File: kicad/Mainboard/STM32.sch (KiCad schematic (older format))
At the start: 30 parts, among them J1 TP1, J11 VIB2, J2 TP2, J3 USB_OTG, J4 SWD, J9 VIB1, Q1 BSS138, Q6 BSS138, U1 STM32F777VIT, U2 USBLC6-2SC6

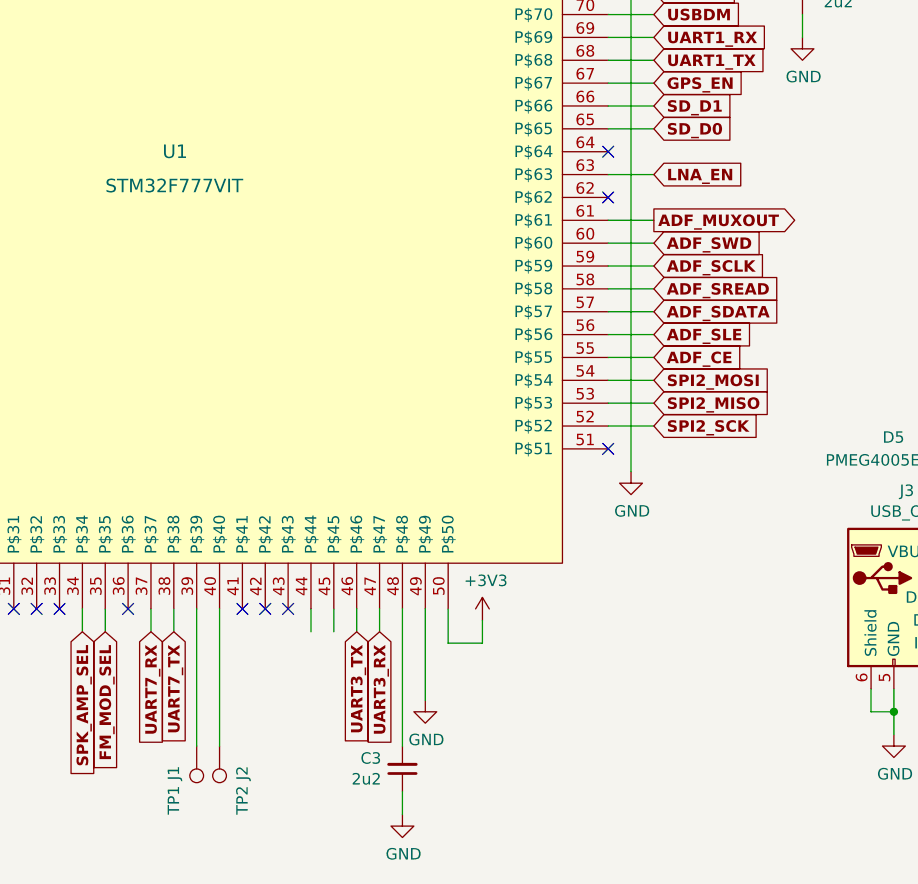
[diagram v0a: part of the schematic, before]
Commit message: Added some vias and forgotten power supply lines & plotted pdf schematic
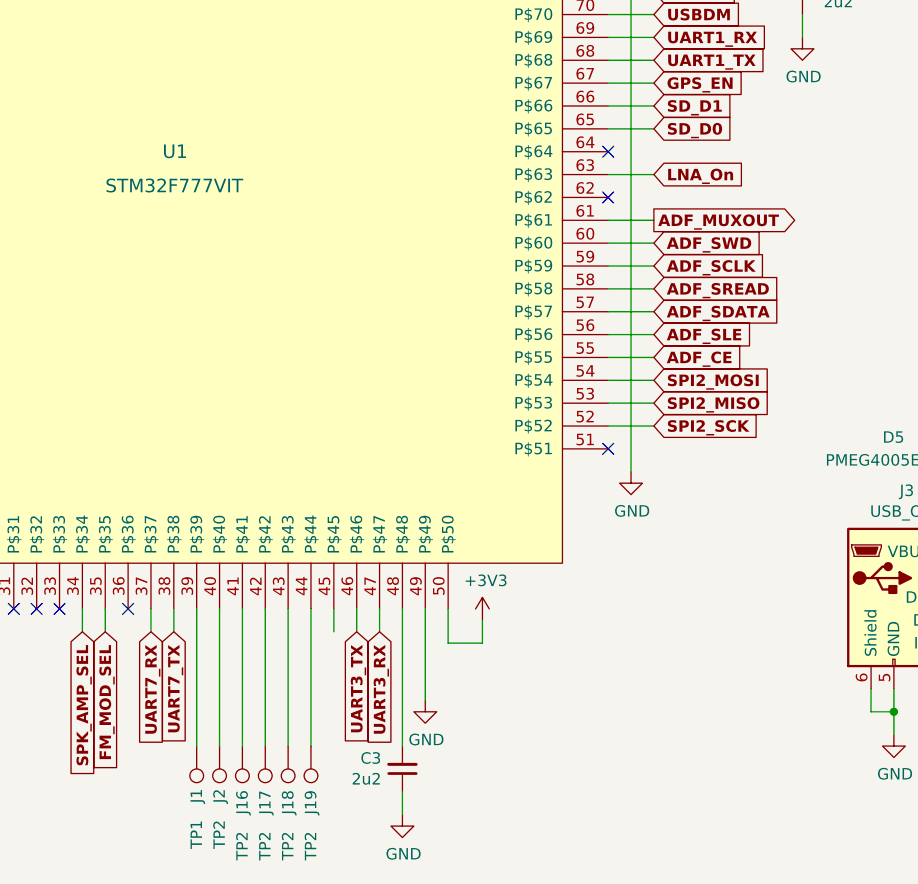
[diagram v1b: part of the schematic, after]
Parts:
- added J16, J17, J18, J19: TP2, TestPoint:TestPoint_Pad_D1.0mm, symbol Mainboard-rescue:TEST_1P-conn
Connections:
- net at U1.41 (P$41): now also J16.1
- net at U1.42 (P$42): now also J17.1
- net at U1.43 (P$43): now also J18.1
- net at U1.44 (P$44): now also J19.1
- net LNA_EN renamed LNA_On
- no-connect marks 28 -> 25
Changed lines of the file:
@@
 EESchema Schematic File Version 4
-LIBS:Mainboard-cache
 EELAYER 30 0
 EELAYER END
@@
 U 1 1 5DE542F9
 P 5100 5950
-F 0 "J1" V 5200 6100 50  0000 R CNN
-F 1 "TP1" V 5200 6250 50  0000 R CNN
+F 0 "J1" V 5100 6200 50  0000 R CNN
+F 1 "TP1" V 5100 6400 50  0000 R CNN
 F 2 "TestPoint:TestPoint_Pad_D1.0mm" H 5300 5950 50  0001 C CNN
 F 3 "" H 5300 5950 50  0001 C CNN
@@
 U 1 1 5DE55232
 P 5200 5950
-F 0 "J2" V 5300 6100 50  0000 R CNN
-F 1 "TP2" V 5300 6250 50  0000 R CNN
+F 0 "J2" V 5200 6200 50  0000 R CNN
+F 1 "TP2" V 5200 6400 50  0000 R CNN
 F 2 "TestPoint:TestPoint_Pad_D1.0mm" H 5400 5950 50  0001 C CNN
 F 3 "" H 5400 5950 50  0001 C CNN
@@
 NoConn ~ 4500 5350
 NoConn ~ 4800 5350
-NoConn ~ 5300 5350
-NoConn ~ 5400 5350
-NoConn ~ 5500 5350
 Wire Wire Line
 	6900 2350 7000 2350
@@
 Wire Wire Line
 	5200 5350 5200 5950
-Wire Wire Line
-	5600 5450 5600 5350
 Text GLabel 4300 1450 1    50   Input ~ 10
 WIFI_RST
@@
 	8500 1300 8600 1300
 Text GLabel 7100 3450 2    50   Input ~ 10
-LNA_EN
+LNA_On
 Wire Wire Line
 	7100 3450 6900 3450
 Wire Wire Line
 	6900 3650 7100 3650
+$Comp
+L Mainboard-rescue:TEST_1P-conn J16
+U 1 1 5EDA6785
+P 5300 5950
+F 0 "J16" V 5300 6250 50  0000 R CNN
+F 1 "TP2" V 5300 6450 50  0000 R CNN
+F 2 "TestPoint:TestPoint_Pad_D1.0mm" H 5500 5950 50  0001 C CNN
+F 3 "" H 5500 5950 50  0001 C CNN
+	1    5300 5950
+	1    0    0    1
+$EndComp
+$Comp
+L Mainboard-rescue:TEST_1P-conn J17
+U 1 1 5EDA8668
+P 5400 5950
+F 0 "J17" V 5400 6250 50  0000 R CNN
+F 1 "TP2" V 5400 6450 50  0000 R CNN
+F 2 "TestPoint:TestPoint_Pad_D1.0mm" H 5600 5950 50  0001 C CNN
+F 3 "" H 5600 5950 50  0001 C CNN
+	1    5400 5950
+	1    0    0    1
+$EndComp
+$Comp
+L Mainboard-rescue:TEST_1P-conn J18
+U 1 1 5EDA889B
+P 5500 5950
+F 0 "J18" V 5500 6250 50  0000 R CNN
+F 1 "TP2" V 5500 6450 50  0000 R CNN
+F 2 "TestPoint:TestPoint_Pad_D1.0mm" H 5700 5950 50  0001 C CNN
+F 3 "" H 5700 5950 50  0001 C CNN
+	1    5500 5950
+	1    0    0    1
+$EndComp
+$Comp
+L Mainboard-rescue:TEST_1P-conn J19
+U 1 1 5EDA8A58
+P 5600 5950
+F 0 "J19" V 5600 6250 50  0000 R CNN
+F 1 "TP2" V 5600 6450 50  0000 R CNN
+F 2 "TestPoint:TestPoint_Pad_D1.0mm" H 5800 5950 50  0001 C CNN
+F 3 "" H 5800 5950 50  0001 C CNN
+	1    5600 5950
+	1    0    0    1
+$EndComp
+Wire Wire Line
+	5300 5350 5300 5950
+Wire Wire Line
+	5400 5950 5400 5350
+Wire Wire Line
+	5500 5350 5500 5950
+Wire Wire Line
+	5600 5350 5600 5950
 $EndSCHEMATC

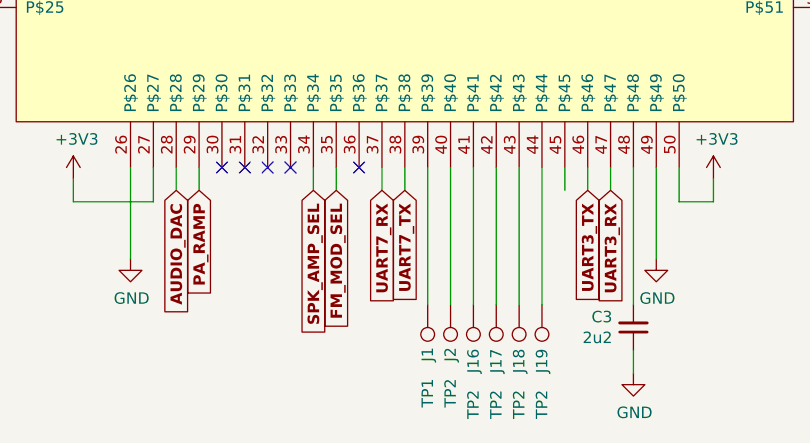
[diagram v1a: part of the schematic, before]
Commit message: added 9 TestPoints called N1 ... to N9, which allow to debug STM32, and experiment with more peripherals in the future. Plotted PDF schematic
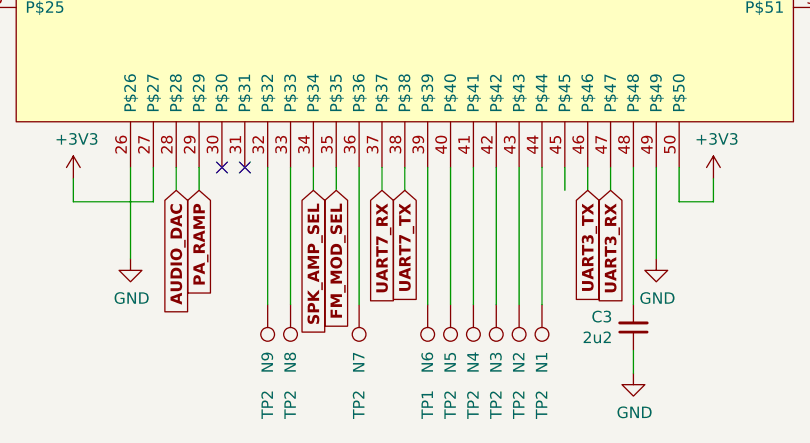
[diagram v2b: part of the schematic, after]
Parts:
- added N7, N8, N9: TP2, TestPoint:TestPoint_Pad_D1.0mm, symbol Mainboard-rescue:TEST_1P-conn
- renumbered J19 to N1, J18 to N2, J17 to N3, J16 to N4, J2 to N5, J1 to N6
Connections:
- net at U1.32 (P$32): now also N9.1
- net at U1.33 (P$33): now also N8.1
- net at U1.36 (P$36): now also N7.1
- no-connect marks 25 -> 22
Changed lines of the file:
@@
 	5900 5350 5900 5450
 $Comp
-L Mainboard-rescue:TEST_1P-conn J1
+L Mainboard-rescue:TEST_1P-conn N6
 U 1 1 5DE542F9
 P 5100 5950
-F 0 "J1" V 5100 6200 50  0000 R CNN
-F 1 "TP1" V 5100 6400 50  0000 R CNN
+F 0 "N6" V 5100 6250 50  0000 R CNN
+F 1 "TP1" V 5100 6450 50  0000 R CNN
 F 2 "TestPoint:TestPoint_Pad_D1.0mm" H 5300 5950 50  0001 C CNN
 F 3 "" H 5300 5950 50  0001 C CNN
@@
 $EndComp
 $Comp
-L Mainboard-rescue:TEST_1P-conn J2
+L Mainboard-rescue:TEST_1P-conn N5
 U 1 1 5DE55232
 P 5200 5950
-F 0 "J2" V 5200 6200 50  0000 R CNN
-F 1 "TP2" V 5200 6400 50  0000 R CNN
+F 0 "N5" V 5200 6250 50  0000 R CNN
+F 1 "TP2" V 5200 6450 50  0000 R CNN
 F 2 "TestPoint:TestPoint_Pad_D1.0mm" H 5400 5950 50  0001 C CNN
 F 3 "" H 5400 5950 50  0001 C CNN
@@
 Wire Wire Line
 	3800 5350 3800 5750
-NoConn ~ 4500 5350
-NoConn ~ 4800 5350
 Wire Wire Line
 	6900 2350 7000 2350
@@
 NoConn ~ 4200 5350
 NoConn ~ 4300 5350
-NoConn ~ 4400 5350
 Wire Wire Line
 	4800 1450 4800 1550
@@
 	6900 3650 7100 3650
 $Comp
-L Mainboard-rescue:TEST_1P-conn J16
+L Mainboard-rescue:TEST_1P-conn N4
 U 1 1 5EDA6785
 P 5300 5950
-F 0 "J16" V 5300 6250 50  0000 R CNN
+F 0 "N4" V 5300 6250 50  0000 R CNN
 F 1 "TP2" V 5300 6450 50  0000 R CNN
 F 2 "TestPoint:TestPoint_Pad_D1.0mm" H 5500 5950 50  0001 C CNN
@@
 $EndComp
 $Comp
-L Mainboard-rescue:TEST_1P-conn J17
+L Mainboard-rescue:TEST_1P-conn N3
 U 1 1 5EDA8668
 P 5400 5950
-F 0 "J17" V 5400 6250 50  0000 R CNN
+F 0 "N3" V 5400 6250 50  0000 R CNN
 F 1 "TP2" V 5400 6450 50  0000 R CNN
 F 2 "TestPoint:TestPoint_Pad_D1.0mm" H 5600 5950 50  0001 C CNN
@@
 $EndComp
 $Comp
-L Mainboard-rescue:TEST_1P-conn J18
+L Mainboard-rescue:TEST_1P-conn N2
 U 1 1 5EDA889B
 P 5500 5950
-F 0 "J18" V 5500 6250 50  0000 R CNN
+F 0 "N2" V 5500 6250 50  0000 R CNN
 F 1 "TP2" V 5500 6450 50  0000 R CNN
 F 2 "TestPoint:TestPoint_Pad_D1.0mm" H 5700 5950 50  0001 C CNN
@@
 $EndComp
 $Comp
-L Mainboard-rescue:TEST_1P-conn J19
+L Mainboard-rescue:TEST_1P-conn N1
 U 1 1 5EDA8A58
 P 5600 5950
-F 0 "J19" V 5600 6250 50  0000 R CNN
+F 0 "N1" V 5600 6250 50  0000 R CNN
 F 1 "TP2" V 5600 6450 50  0000 R CNN
 F 2 "TestPoint:TestPoint_Pad_D1.0mm" H 5800 5950 50  0001 C CNN
@@
 Wire Wire Line
 	5600 5350 5600 5950
+$Comp
+L Mainboard-rescue:TEST_1P-conn N7
+U 1 1 5EE3107D
+P 4800 5950
+F 0 "N7" V 4800 6250 50  0000 R CNN
+F 1 "TP2" V 4800 6450 50  0000 R CNN
+F 2 "TestPoint:TestPoint_Pad_D1.0mm" H 5000 5950 50  0001 C CNN
+F 3 "" H 5000 5950 50  0001 C CNN
+	1    4800 5950
+	1    0    0    1
+$EndComp
+$Comp
+L Mainboard-rescue:TEST_1P-conn N8
+U 1 1 5EE31358
+P 4500 5950
+F 0 "N8" V 4500 6250 50  0000 R CNN
+F 1 "TP2" V 4500 6450 50  0000 R CNN
+F 2 "TestPoint:TestPoint_Pad_D1.0mm" H 4700 5950 50  0001 C CNN
+F 3 "" H 4700 5950 50  0001 C CNN
+	1    4500 5950
+	1    0    0    1
+$EndComp
+$Comp
+L Mainboard-rescue:TEST_1P-conn N9
+U 1 1 5EE317B2
+P 4400 5950
+F 0 "N9" V 4400 6250 50  0000 R CNN
+F 1 "TP2" V 4400 6450 50  0000 R CNN
+F 2 "TestPoint:TestPoint_Pad_D1.0mm" H 4600 5950 50  0001 C CNN
+F 3 "" H 4600 5950 50  0001 C CNN
+	1    4400 5950
+	1    0    0    1
+$EndComp
+Wire Wire Line
+	4800 5350 4800 5950
+Wire Wire Line
+	4500 5350 4500 5950
+Wire Wire Line
+	4400 5350 4400 5950
 $EndSCHEMATC

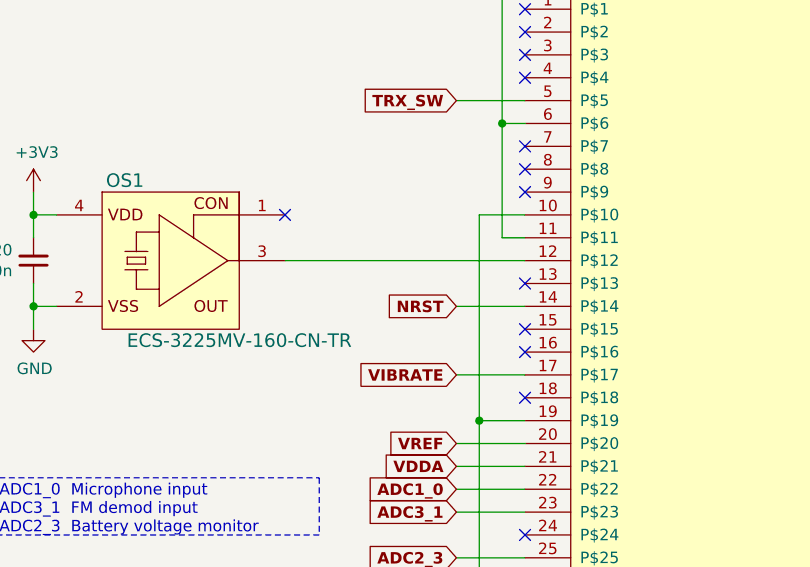
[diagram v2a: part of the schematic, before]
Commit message: added jumpers on GPIO0 and GPIO2 for ESP8266 module; described pin headers on PCB; connected pin 16 of STM32 to Power Down pin in OS1; plotted schematic in PDF
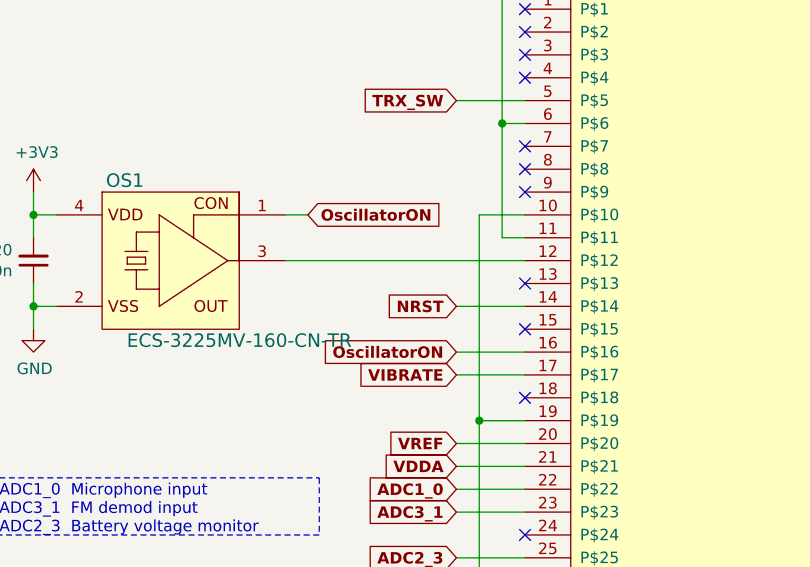
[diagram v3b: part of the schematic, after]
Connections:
- net OscillatorON: now reaches OS1.1 (CON)
- net OscillatorON: now also U1.16 (P$16)
- no-connect marks 22 -> 20
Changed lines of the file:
@@
 	1    0    0    -1
 $EndComp
-NoConn ~ 2050 3150
 $Comp
 L TR-9:STM32F777VIT U1
@@
 NoConn ~ 3100 3450
 NoConn ~ 3100 3650
-NoConn ~ 3100 3750
 NoConn ~ 3100 3950
 NoConn ~ 3100 4550
@@
 Wire Wire Line
 	4400 5350 4400 5950
+Text GLabel 2800 3750 0    50   Input ~ 10
+OscillatorON
+Wire Wire Line
+	3100 3750 2800 3750
+Text GLabel 2150 3150 2    50   Input ~ 10
+OscillatorON
+Wire Wire Line
+	2150 3150 2050 3150
 $EndSCHEMATC

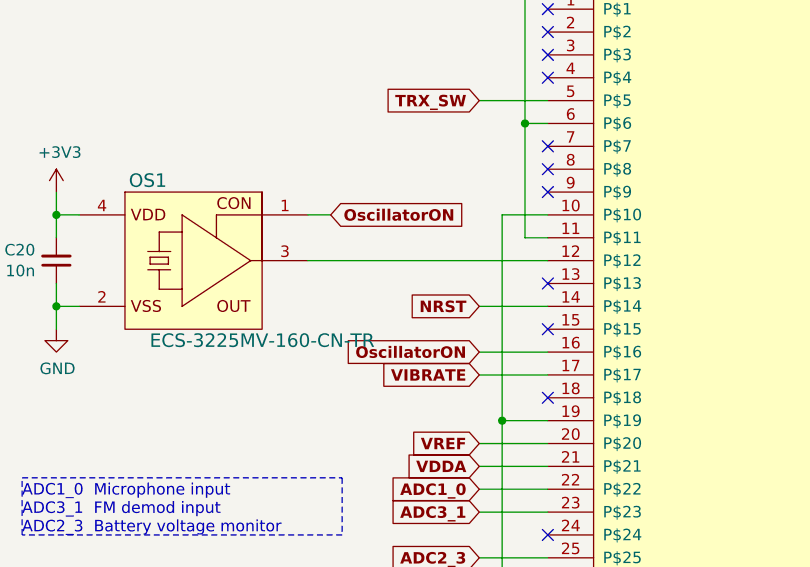
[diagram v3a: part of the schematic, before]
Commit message: changed OscillatorON to XO_EN -> added "SN:" title on PCB -> plotted new PDF
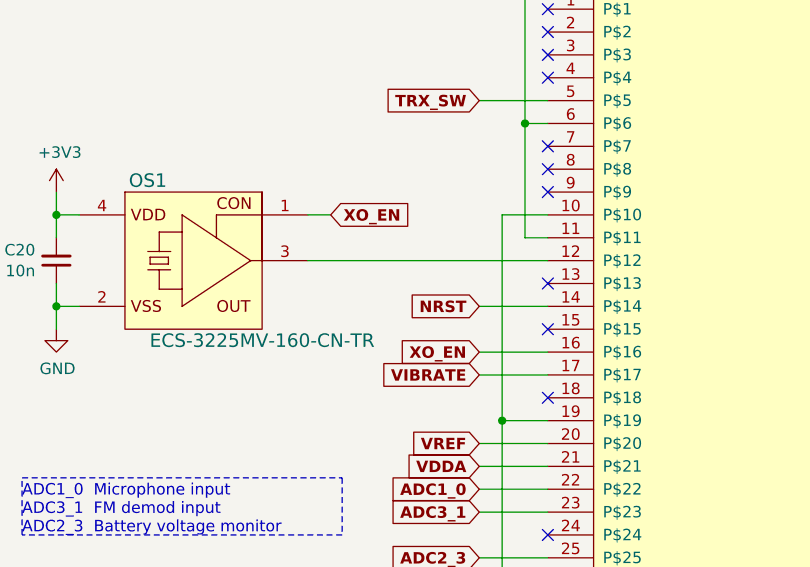
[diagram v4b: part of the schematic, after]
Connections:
- net OscillatorON renamed XO_EN
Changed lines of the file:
@@
 	4400 5350 4400 5950
 Text GLabel 2800 3750 0    50   Input ~ 10
-OscillatorON
+XO_EN
 Wire Wire Line
 	3100 3750 2800 3750
 Text GLabel 2150 3150 2    50   Input ~ 10
-OscillatorON
+XO_EN
 Wire Wire Line
 	2150 3150 2050 3150

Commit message: added few values in BOM
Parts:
- C1, C2, C3, C4: Tolerance (none) -> 10; Voltage (none) -> 25
- C20, C5: value 10n -> 10n; Tolerance (none) -> 10; Voltage (none) -> 25
- C6, C7: Tolerance (none) -> 2; Voltage (none) -> 25
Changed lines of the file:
@@
 U 1 1 5DE325EB
 P 1400 1750
-F 0 "C1" H 1492 1796 50  0000 L CNN
-F 1 "100n" H 1492 1705 50  0000 L CNN
+F 0 "C1" V 1250 1600 50  0000 L CNN
+F 1 "100n" V 1550 1400 50  0000 L CNN
 F 2 "Capacitor_SMD:C_0603_1608Metric" H 1400 1750 50  0001 C CNN
 F 3 "~" H 1400 1750 50  0001 C CNN
+F 4 "25" V 1400 1750 50  0001 C CNN "Voltage"
+F 5 "10" V 1400 1750 50  0001 C CNN "Tolerance"
 	1    1400 1750
 	1    0    0    -1
@@
 U 1 1 5DE32C17
 P 1800 1750
-F 0 "C2" H 1892 1796 50  0000 L CNN
-F 1 "100n" H 1892 1705 50  0000 L CNN
+F 0 "C2" V 1700 1600 50  0000 L CNN
+F 1 "100n" V 1950 1400 50  0000 L CNN
 F 2 "Capacitor_SMD:C_0603_1608Metric" H 1800 1750 50  0001 C CNN
 F 3 "~" H 1800 1750 50  0001 C CNN
+F 4 "25" H 1800 1750 50  0001 C CNN "Voltage"
+F 5 "10" H 1800 1750 50  0001 C CNN "Tolerance"
 	1    1800 1750
 	1    0    0    -1
@@
 F 2 "Capacitor_SMD:C_0603_1608Metric" H 6000 6050 50  0001 C CNN
 F 3 "~" H 6000 6050 50  0001 C CNN
+F 4 "10" H 6000 6050 50  0001 C CNN "Tolerance"
+F 5 "25" H 6000 6050 50  0001 C CNN "Voltage"
 	1    6000 6050
 	1    0    0    1
@@
 F 2 "Capacitor_SMD:C_0603_1608Metric" H 7750 2650 50  0001 C CNN
 F 3 "~" H 7750 2650 50  0001 C CNN
+F 4 "10" H 7750 2650 50  0001 C CNN "Tolerance"
+F 5 "25" H 7750 2650 50  0001 C CNN "Voltage"
 	1    7750 2650
 	-1   0    0    1
@@
 U 1 1 5DEE56A1
 P 8550 5700
-F 0 "C5" H 8458 5654 50  0000 R CNN
-F 1 "10n" H 8458 5745 50  0000 R CNN
+F 0 "C5" V 8650 5850 50  0000 R CNN
+F 1 "10n " V 8450 6000 50  0000 R CNN
 F 2 "Capacitor_SMD:C_0603_1608Metric" H 8550 5700 50  0001 C CNN
 F 3 "~" H 8550 5700 50  0001 C CNN
+F 4 "25" V 8550 5700 50  0001 C CNN "Voltage"
+F 5 "10" H 8550 5700 50  0001 C CNN "Tolerance"
 	1    8550 5700
 	1    0    0    1
@@
 F 2 "Capacitor_SMD:C_0603_1608Metric" H 10150 5900 50  0001 C CNN
 F 3 "~" H 10150 5900 50  0001 C CNN
+F 4 "2" H 10150 5900 50  0001 C CNN "Tolerance"
+F 5 "25" H 10150 5900 50  0001 C CNN "Voltage"
 	1    10150 5900
 	1    0    0    1
@@
 F 2 "Capacitor_SMD:C_0603_1608Metric" H 10350 5900 50  0001 C CNN
 F 3 "~" H 10350 5900 50  0001 C CNN
+F 4 "2" H 10350 5900 50  0001 C CNN "Tolerance"
+F 5 "25" H 10350 5900 50  0001 C CNN "Voltage"
 	1    10350 5900
 	-1   0    0    1
@@
 U 1 1 5E604107
 P 950 3350
-F 0 "C20" H 858 3304 50  0000 R CNN
-F 1 "10n" H 858 3395 50  0000 R CNN
+F 0 "C20" V 850 3550 50  0000 R CNN
+F 1 "10n " V 1050 3550 50  0000 R CNN
 F 2 "Capacitor_SMD:C_0603_1608Metric" H 950 3350 50  0001 C CNN
 F 3 "~" H 950 3350 50  0001 C CNN
+F 4 "10" H 950 3350 50  0001 C CNN "Tolerance"
+F 5 "25" H 950 3350 50  0001 C CNN "Voltage"
 	1    950  3350
 	1    0    0    1
